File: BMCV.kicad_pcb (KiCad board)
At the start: 4 copper layers, 80 x 108 mm, 349 parts, among them J1 AudioJack2_SwitchT, J10 AudioJack2_SwitchT, J11 AudioJack2_SwitchT, J12 AudioJack2_SwitchT, J13 DebugPins, J14 USB_C_Receptacle_USB2.0_14P, J16 Conn_02x08_Eurorack, J2 AudioJack2_SwitchT, J3 AudioJack2_SwitchT, J4 AudioJack2_SwitchT, J5 AudioJack2_SwitchT, J6 AudioJack2_SwitchT, J7 AudioJack2_SwitchT, J8 AudioJack2_SwitchT, J9 AudioJack2_SwitchT, SW1 TC002-N11AS2XT-RGB, SW10 TC002-N11AS2XT-RGB, SW11 TC002-N11AS2XT-RGB, SW12 TC002-N11AS2XT-RGB, SW13 TC002-N11AS2XT-RGB, SW14 Reset, SW15 Boot, SW2 TC002-N11AS2XT-RGB, SW3 TC002-N11AS2XT-RGB, SW4 TC002-N11AS2XT-RGB, SW5 TC002-N11AS2XT-RGB, SW6 TC002-N11AS2XT-RGB, SW7 TC002-N11AS2XT-RGB, SW8 TC002-N11AS2XT-RGB, SW9 TC002-N11AS2XT-RGB, U1 PEL12T-4225S-S1024, U10 WS2811F, U11 WS2811F, U12 WS2811F, U13 WS2811F, U14 WS2811F, U15 WS2811F, U16 WS2811F, U17 WS2811F, U18 WS2811F, U19 WS2811F, U2 PEL12T-4225S-S1024, U20 WS2811F, U21 WS2811F, U22 WS2811F, U23 WS2811F, U24 WS2811F, U25 WS2811F, U26 WS2811F, U27 WS2811F, U28 WS2811F, U29 WS2811F, U3 PEL12T-4225S-S1024, U30 MCP23S17_SS, U31 MCP23S17_SS, U32 TXS0108EPW, U33 AD7367-5, U34 AD5734R, U35 AD5734R, U36 STM32G474CETx, U38 OPA4171, U39 OPA4171, U4 PEL12T-4225S-S1024, U40 OPA4171, U41 TLV76733, U5 PEL12T-4225S-S1024, U6 PEL12T-4225S-S1024, U7 PEL12T-4225S-S1024, U8 PEL12T-4225S-S1024, U9 WS2811F, Y1 38.4MHz 10pF

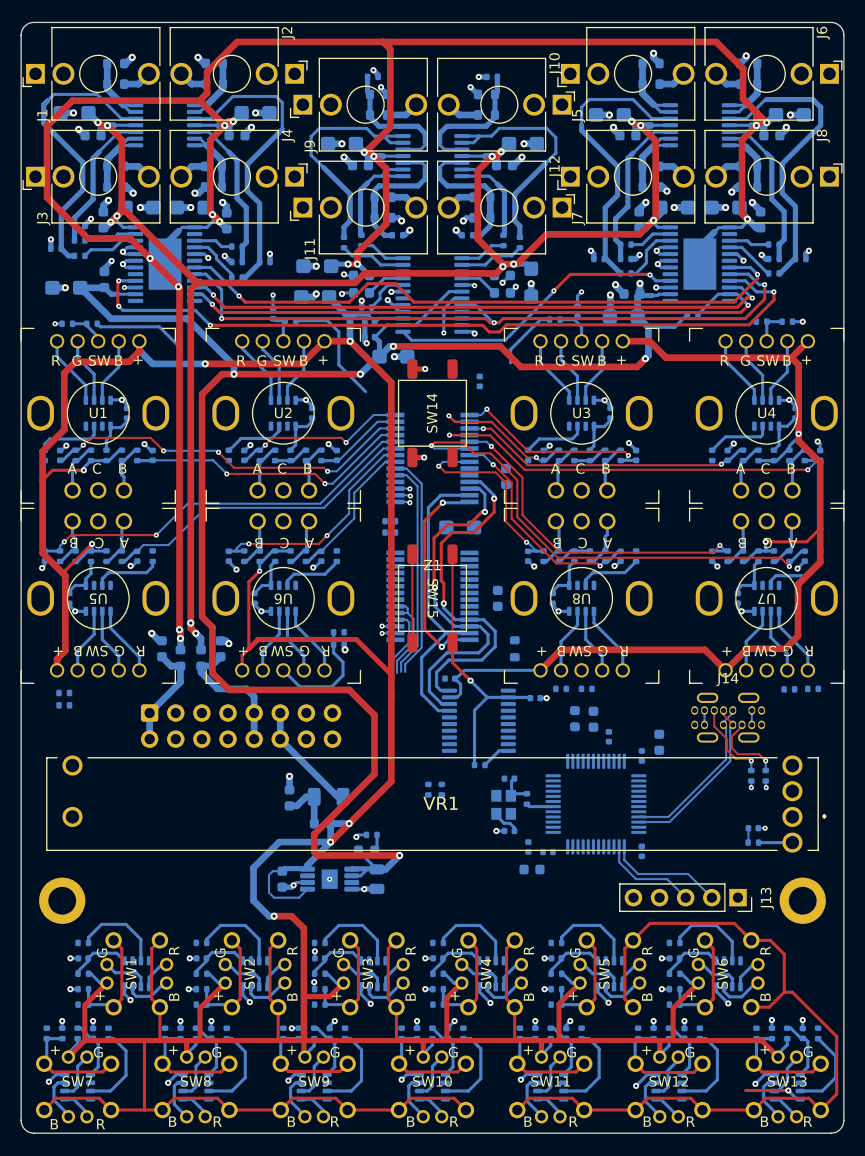
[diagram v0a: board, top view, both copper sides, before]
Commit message: switches & led data routing
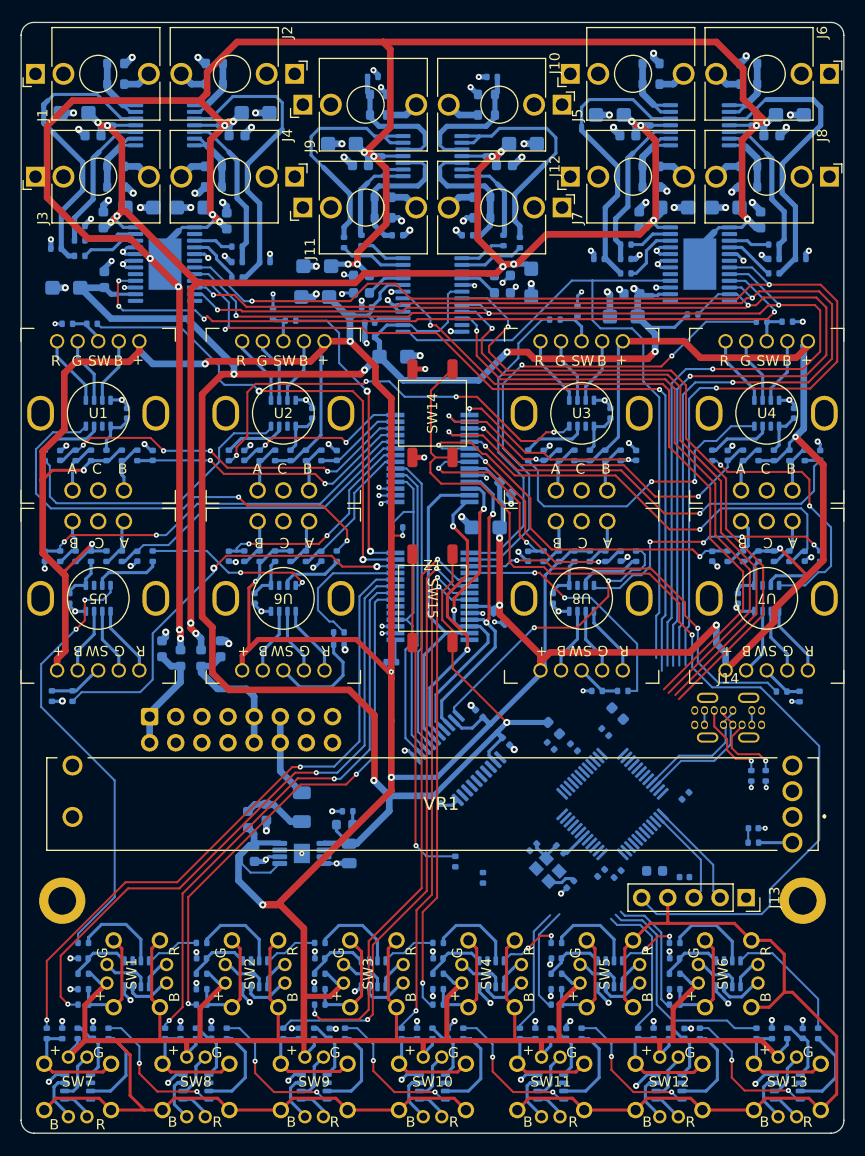
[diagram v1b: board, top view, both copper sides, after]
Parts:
- removed R164: 100, Resistor_SMD:R_0603_1608Metric
- C9: footprint Capacitor_SMD:C_0603_1608Metric -> Capacitor_SMD:C_0402_1005Metric
- moved C11 52.1 mm to (94.5, 113.1), turned to 180 degrees
- moved R160 12.6 mm to (66.0, 92.2), turned to 0 degrees
- moved C7 11.9 mm to (91.6, 112.5), turned to 0 degrees
- moved R163 9.46 mm to (74.9, 113.2)
- moved C1 7.86 mm to (83.4, 113.8), turned to -135 degrees
- moved Y1 7.64 mm to (81.2, 112.4), turned to 135 degrees
- moved C4 7.51 mm to (86.4, 112.7), turned to -135 degrees
- moved R3 7.46 mm to (72.2, 111.6), turned to 90 degrees
- moved FB2 7.26 mm to (52.0, 107.5), turned to 90 degrees
- moved C3 7.10 mm to (88.0, 112.8), turned to -135 degrees
- moved C2 7.06 mm to (79.8, 110.2), turned to -135 degrees
- moved C5 6.87 mm to (94.6, 105.2), turned to 45 degrees
- moved R136 6.00 mm to (88.5, 95.0), turned to 0 degrees
- moved R41 5.86 mm to (82.4, 110.4), turned to -45 degrees
- moved R162 5.38 mm to (70.4, 105.6), turned to 135 degrees
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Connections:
- R140 pad 2: unconnected-(R140-Pad2) -> BTN_MCU_2
- R141 pad 2: unconnected-(R141-Pad2) -> BTN_MCU_5
- R142 pad 2: unconnected-(R142-Pad2) -> BTN_MCU_4
- R143 pad 2: unconnected-(R143-Pad2) -> BTN_MCU_3
- R144 pad 2: unconnected-(R144-Pad2) -> BTN_MCP_8
- R145 pad 2: /Buttons/BUTTON_MCU_5 -> BTN_MCP_7
- R146 pad 2: /Buttons/BUTTON_MCU_4 -> BTN_MCP_6
- R147 pad 2: /Buttons/BUTTON_MCU_3 -> BTN_MCP_5
- R148 pad 2: unconnected-(R148-Pad2) -> BTN_MCU_1
- R150 pad 2: unconnected-(R150-Pad2) -> BTN_MCP_4
- R152 pad 2: unconnected-(R152-Pad2) -> BTN_MCP_3
- R154 pad 2: /Buttons/BUTTON_MCU_2 -> BTN_MCP_2
- R156 pad 2: /Buttons/BUTTON_MCU_1 -> BTN_MCP_1
- R42 pad 2: unconnected-(R42-Pad2) -> Net-(U10-DO)
- R64 pad 2: unconnected-(R64-Pad2) -> Net-(U11-DO)
- R65 pad 2: unconnected-(R65-Pad2) -> Net-(U12-DO)
- R66 pad 2: unconnected-(R66-Pad2) -> Net-(U15-DO)
- R67 pad 2: unconnected-(R67-Pad2) -> WSDATA_5V
- R68 pad 2: unconnected-(R68-Pad2) -> Net-(U16-DO)
- R69 pad 2: unconnected-(R69-Pad2) -> Net-(U9-DO)
- R70 pad 2: unconnected-(R70-Pad2) -> Net-(U14-DO)
- R71 pad 2: unconnected-(R71-Pad2) -> WSDATA_5V_BOTTOM
- R72 pad 2: unconnected-(R72-Pad2) -> Net-(U17-DO)
- R73 pad 2: unconnected-(R73-Pad2) -> Net-(U18-DO)
- R74 pad 2: unconnected-(R74-Pad2) -> Net-(U19-DO)
- R75 pad 2: unconnected-(R75-Pad2) -> Net-(U20-DO)
- R76 pad 2: unconnected-(R76-Pad2) -> Net-(U21-DO)
- R77 pad 2: unconnected-(R77-Pad2) -> Net-(U22-DO)
- R78 pad 2: unconnected-(R78-Pad2) -> Net-(U29-DO)
- R79 pad 2: unconnected-(R79-Pad2) -> Net-(U28-DO)
- R80 pad 2: unconnected-(R80-Pad2) -> Net-(U27-DO)
- R81 pad 2: unconnected-(R81-Pad2) -> Net-(U26-DO)
- R82 pad 2: unconnected-(R82-Pad2) -> Net-(U25-DO)
- R83 pad 2: unconnected-(R83-Pad2) -> Net-(U24-DO)
- U10 pad 5: unconnected-(U10-DO-Pad5) -> Net-(U10-DO)
- U11 pad 5: unconnected-(U11-DO-Pad5) -> Net-(U11-DO)
- U12 pad 5: unconnected-(U12-DO-Pad5) -> Net-(U12-DO)
- U13 pad 5: unconnected-(U13-DO-Pad5) -> WSDATA_5V_BOTTOM
- U14 pad 5: unconnected-(U14-DO-Pad5) -> Net-(U14-DO)
- U15 pad 5: unconnected-(U15-DO-Pad5) -> Net-(U15-DO)
- U16 pad 5: unconnected-(U16-DO-Pad5) -> Net-(U16-DO)
- U17 pad 5: unconnected-(U17-DO-Pad5) -> Net-(U17-DO)
- U18 pad 5: unconnected-(U18-DO-Pad5) -> Net-(U18-DO)
- U19 pad 5: unconnected-(U19-DO-Pad5) -> Net-(U19-DO)
- U20 pad 5: unconnected-(U20-DO-Pad5) -> Net-(U20-DO)
- U21 pad 5: unconnected-(U21-DO-Pad5) -> Net-(U21-DO)
- U22 pad 5: unconnected-(U22-DO-Pad5) -> Net-(U22-DO)
- U24 pad 5: unconnected-(U24-DO-Pad5) -> Net-(U24-DO)
- U25 pad 5: unconnected-(U25-DO-Pad5) -> Net-(U25-DO)
- U26 pad 5: unconnected-(U26-DO-Pad5) -> Net-(U26-DO)
- U27 pad 5: unconnected-(U27-DO-Pad5) -> Net-(U27-DO)
- U28 pad 5: unconnected-(U28-DO-Pad5) -> Net-(U28-DO)
- U29 pad 5: unconnected-(U29-DO-Pad5) -> Net-(U29-DO)
- U30 pad 1: ENC_1_SW -> ENC_2_SW
- U30 pad 19: MCP_5V_BTNINT -> unconnected-(U30-INTB-Pad19)
- U30 pad 2: ENC_2_SW -> ENC_1_SW
- U30 pad 20: MCP_5V_BTNINT -> unconnected-(U30-INTA-Pad20)
- U30 pad 21: unconnected-(U30-GPA0-Pad21) -> BTN_MCP_2
- U30 pad 22: unconnected-(U30-GPA1-Pad22) -> BTN_MCP_6
- U30 pad 23: unconnected-(U30-GPA2-Pad23) -> BTN_MCP_1
- U30 pad 24: unconnected-(U30-GPA3-Pad24) -> BTN_MCP_5
- U30 pad 25: unconnected-(U30-GPA4-Pad25) -> ENC_6_SW
- U30 pad 26: unconnected-(U30-GPA5-Pad26) -> ENC_5_SW
- U30 pad 27: unconnected-(U30-GPA6-Pad27) -> ENC_4_SW
- U30 pad 28: unconnected-(U30-GPA7-Pad28) -> ENC_3_SW
- U30 pad 3: ENC_3_SW -> ENC_7_SW
- U30 pad 4: ENC_4_SW -> ENC_8_SW
- U30 pad 5: ENC_5_SW -> BTN_MCP_3
- U30 pad 6: ENC_6_SW -> BTN_MCP_7
- U30 pad 7: ENC_7_SW -> BTN_MCP_8
- U30 pad 8: ENC_8_SW -> BTN_MCP_4
- U31 pad 5: ENC_7_B -> ENC_7_A
- U31 pad 6: ENC_7_A -> ENC_7_B
- U32 pad 1: MCP_CS -> WSDATA
- U32 pad 12: WSDATA_5V -> MCP_5V_RESET
- U32 pad 13: unconnected-(U32-B7-Pad13) -> MCP_5V_ENCINT_A
- U32 pad 14: unconnected-(U32-B6-Pad14) -> MCP_5V_ENCINT_B
- U32 pad 15: MCP_5V_RESET -> MCP_5V_SI
- U32 pad 16: unconnected-(U32-B4-Pad16) -> MCP_5V_SO
- U32 pad 17: MCP_5V_SI -> MCP_5V_SCK
- U32 pad 18: MCP_5V_SCK -> MCP_5V_CS
- U32 pad 20: MCP_5V_CS -> WSDATA_5V
- U32 pad 3: MCP_SCK -> MCP_CS
- U32 pad 4: MCP_SI -> MCP_SCK
- U32 pad 5: unconnected-(U32-A4-Pad5) -> MCP_SO
- U32 pad 6: MCP_RESET -> MCP_SI
- U32 pad 7: unconnected-(U32-A6-Pad7) -> MCP_ENCINT_B
- U32 pad 8: unconnected-(U32-A7-Pad8) -> MCP_ENCINT_A
- U32 pad 9: WSDATA -> MCP_RESET
- U36 pad 10: unconnected-(U36-PA2-Pad10) -> ADC_DAC_SDO
- U36 pad 11: unconnected-(U36-PA3-Pad11) -> ADC_DAC_SDIN
- U36 pad 12: unconnected-(U36-PA4-Pad12) -> ADC_DAC_SCLK
- U36 pad 13: unconnected-(U36-PA5-Pad13) -> ADC_CS
- U36 pad 14: unconnected-(U36-PA6-Pad14) -> ADC_ADDR
- U36 pad 15: unconnected-(U36-PA7-Pad15) -> ADC_CNVST
- U36 pad 25: unconnected-(U36-PB11-Pad25) -> BTN_MCU_1
- U36 pad 26: unconnected-(U36-PB12-Pad26) -> BTN_MCU_2
- U36 pad 27: unconnected-(U36-PB13-Pad27) -> BTN_MCU_3
- U36 pad 28: unconnected-(U36-PB14-Pad28) -> BTN_MCU_4
- U36 pad 29: unconnected-(U36-PB15-Pad29) -> BTN_MCU_5
- U36 pad 30: unconnected-(U36-PA8-Pad30) -> ADC_BUSY
- U36 pad 31: unconnected-(U36-PA9-Pad31) -> DAC_1_SYNC
- U36 pad 32: unconnected-(U36-PA10-Pad32) -> DAC_1_LDAC
- U36 pad 39: unconnected-(U36-PA15-Pad39) -> DAC_1_CLR
- U9 pad 5: unconnected-(U9-DO-Pad5) -> Net-(U9-DO)
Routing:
- net NRST: track 0.00 -> 98.6 mm, vias 0 -> 1
- net ADC_DAC_SDIN: track 0.00 -> 79.5 mm, vias 0 -> 2
- net +5V: track 576.9 -> 656.0 mm, vias 10 -> 14
- net ADC_ADDR: track 0.00 -> 65.2 mm, vias 0 -> 1
- net BTN_MCP_5: track 0.00 -> 64.1 mm, vias 0 -> 2
- net ADC_CNVST: track 0.00 -> 63.4 mm, vias 0 -> 1
- net ADC_CS: track 4.54 -> 66.8 mm
- net BTN_MCP_1: track 0.00 -> 61.8 mm, vias 0 -> 2
- net ADC_BUSY: track 0.00 -> 61.1 mm, vias 0 -> 1
- net BTN_MCP_7: track 0.00 -> 59.1 mm, vias 0 -> 2
- net BTN_MCP_3: track 0.00 -> 57.3 mm, vias 0 -> 2
- net DAC_1_SYNC: track 62.0 -> 118.8 mm, vias 2 -> 3
- net DAC_1_LDAC: track 58.1 -> 114.3 mm, vias 2 -> 3
- net DAC_1_CLR: track 61.1 -> 116.8 mm, vias 2 -> 3
- net BTN_MCP_6: track 0.00 -> 55.1 mm, vias 0 -> 2
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
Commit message: completed routing and mcu pins
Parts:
- removed R41: 33, Resistor_SMD:R_0402_1005Metric
- added C95: 100n, Capacitor_SMD:C_0402_1005Metric, B.Cu at (95.0, 107.0)
- added J15: Conn_01x02, TestPoint:TestPoint_2Pads_Pitch2.54mm_Drill0.8mm, B.Cu at (73.6, 114.2)
- added U37: MB85RS64PNF-G-JNERE1, Package_SO:SSOP-8_3.9x5.05mm_P1.27mm, B.Cu at (98.5, 108.8)
- moved C11 20.8 mm to (107.0, 96.5), turned to -90 degrees
- moved R158 7.98 mm to (96.7, 103.2), turned to -90 degrees
- moved C46 6.05 mm to (99.0, 102.7)
- moved R163 3.88 mm to (75.6, 109.3)
- moved R3 2.92 mm to (74.1, 109.3)
- moved C1 1.62 mm to (84.0, 112.3), turned to -90 degrees
- moved C2 1.57 mm to (81.2, 109.6), turned to 180 degrees
- moved C10 0.99 mm to (87.2, 97.7)
- moved Y1 0.83 mm to (81.7, 111.7), turned to 180 degrees
- moved C5 0.54 mm to (94.3, 104.8)
- moved C4 0.54 mm to (86.9, 112.5)
- moved C7 0.52 mm to (91.1, 112.3)
- moved C6 0.34 mm to (86.5, 99.2)
- moved C3 0.32 mm to (88.1, 113.1)
- moved C8 0.24 mm to (84.0, 100.3), turned to 45 degrees
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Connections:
- C2 pad 1: Net-(C2-Pad1) -> HSE_OUT
- R163 pad 1: BOOT -> Net-(R163-Pad1)
- R163 pad 2: Net-(U36-PB8) -> BOOT
- R3 pad 2: BOOT -> Net-(R163-Pad1)
- SW15 pad 2: BOOT -> Net-(R163-Pad1)
- U36 pad 10: ADC_DAC_SDO -> MCP_ENCINT_A
- U36 pad 11: ADC_DAC_SDIN -> MCP_ENCINT_B
- U36 pad 12: ADC_DAC_SCLK -> MCP_CS
- U36 pad 13: ADC_CS -> MCP_SCK
- U36 pad 14: ADC_ADDR -> MCP_SO
- U36 pad 15: ADC_CNVST -> MCP_SI
- U36 pad 16: unconnected-(U36-PB0-Pad16) -> MCP_RESET
- U36 pad 17: unconnected-(U36-PB1-Pad17) -> WSDATA
- U36 pad 18: unconnected-(U36-PB2-Pad18) -> ADC_CS
- U36 pad 2: unconnected-(U36-PC13-Pad2) -> BTN_MCU_2
- U36 pad 22: unconnected-(U36-PB10-Pad22) -> ADC_CNVST
- U36 pad 25: BTN_MCU_1 -> ADC_ADDR
- U36 pad 26: BTN_MCU_2 -> ADC_BUSY
- U36 pad 27: BTN_MCU_3 -> ADC_DAC_SCLK
- U36 pad 28: BTN_MCU_4 -> ADC_DAC_SDO
- U36 pad 29: BTN_MCU_5 -> ADC_DAC_SDIN
- U36 pad 3: unconnected-(U36-PC14-Pad3) -> BTN_MCU_5
- U36 pad 30: ADC_BUSY -> DAC_1_CLR
- U36 pad 31: DAC_1_SYNC -> DAC_1_LDAC
- U36 pad 32: DAC_1_LDAC -> DAC_1_SYNC
- U36 pad 39: DAC_1_CLR -> EXP_CS
- U36 pad 4: unconnected-(U36-PC15-Pad4) -> BTN_MCU_4
- U36 pad 43: unconnected-(U36-PB6-Pad43) -> PB6
- U36 pad 44: unconnected-(U36-PB7-Pad44) -> PB7
- U36 pad 45: Net-(U36-PB8) -> BOOT
- U36 pad 46: unconnected-(U36-PB9-Pad46) -> BTN_MCU_1
- U36 pad 8: unconnected-(U36-PA0-Pad8) -> BTN_MCU_3
- VR1 pad 1: +3.3VA -> +3.3V
- Y1 pad 3: Net-(C2-Pad1) -> HSE_OUT
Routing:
- net +3.3V: track 292.2 -> 369.6 mm, vias 7 -> 10
- net Net-(R163-Pad1): track 0.00 -> 42.4 mm, vias 0 -> 1
- net GND: track 201.5 -> 230.0 mm, vias 167 -> 193
- net PB6: track 0.00 -> 25.1 mm, vias 0 -> 1
- net PB7: track 0.00 -> 20.4 mm, vias 0 -> 1
- net NRST: track 98.6 -> 117.6 mm, vias 1 -> 2
- net BOOT: track 32.7 -> 16.6 mm, vias 1 -> 2
- net ADC1_IN2_SLIDER: track 1.41 -> 17.1 mm, vias 0 -> 2
- net ADC_CS: track 66.8 -> 82.0 mm, vias 1 -> 2
- net EXP_MISO: track 0.00 -> 14.4 mm
- net MCP_RESET: track 0.00 -> 14.0 mm, vias 0 -> 2
- net BTN_MCU_3: track 12.2 -> 25.5 mm, vias 0 -> 2
- net ADC_CNVST: track 63.4 -> 76.2 mm, vias 1 -> 2
- net DAC_1_LDAC: track 114.3 -> 126.5 mm
- net ADC_DAC_SCLK: track 120.5 -> 132.6 mm, vias 4 -> 6
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
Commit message: cleanup
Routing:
- net Net-(VR1-WIPER): track 12.2 -> 10.8 mm
- net EXP_SCLK: track 7.25 -> 6.75 mm
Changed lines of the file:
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@@
 	)
 	(segment
-		(start 90.175 112.2)
-		(end 90.325 112.35)
-		(width 0.5)
-		(layer "B.Cu")
-		(net 39)
-	)
-	(segment
 		(start 92.125 56.425)
 		(end 93.125 56.425)
@@
 	)
 	(segment
-		(start 100.790523 107.357502)
-		(end 100.790523 107.359477)
-		(width 0.2)
-		(layer "B.Cu")
-		(net 39)
-	)
-	(segment
 		(start 91.4 56.55)
 		(end 92 56.55)
@@
 	)
 	(segment
-		(start 96.109477 110.242498)
-		(end 96.157502 110.242498)
-		(width 0.2)
-		(layer "B.Cu")
-		(net 39)
-	)
-	(segment
 		(start 83.943153 97.943153)
 		(end 85.75 99.75)
@@
 	)
 	(segment
-		(start 94.660589 107.289411)
-		(end 94.55 107.178822)
-		(width 0.3)
-		(layer "B.Cu")
-		(net 39)
-	)
-	(segment
 		(start 50.7 63.35)
 		(end 46.15 58.8)
@@
 	)
 	(segment
-		(start 80.67 109.6)
-		(end 80.72 109.55)
-		(width 0.3)
-		(layer "B.Cu")
-		(net 65)
-	)
-	(segment
 		(start 40.9 46.6)
 		(end 40.3 46)
@@
 	)
 	(segment
-		(start 102.41 103.75)
-		(end 102.4 103.76)
-		(width 0.2)
-		(layer "B.Cu")
-		(net 65)
-	)
-	(segment
 		(start 86.425 113.675)
 		(end 86.560589 113.539411)
@@
 	)
 	(segment
-		(start 101.688549 108.255528)
-		(end 101.688549 108.261451)
-		(width 0.3)
-		(layer "B.Cu")
-		(net 65)
-	)
-	(segment
 		(start 74.4 37)
 		(end 73.7 36.3)
@@
 	)
 	(segment
-		(start 96.65 102.69)
-		(end 96.64 102.7)
-		(width 0.2)
-		(layer "B.Cu")
-		(net 110)
-	)
-	(segment
-		(start 98.57 102.7)
-		(end 98.56 102.69)
-		(width 0.2)
-		(layer "B.Cu")
-		(net 110)
-	)
-	(segment
 		(start 40.3 68.8)
 		(end 39.7 69.4)
@@
 	)
 	(segment
-		(start 104.15 109.75)
-		(end 105 109.75)
-		(width 0.2)
-		(layer "B.Cu")
-		(net 255)
-	)
-	(segment
-		(start 104.42 109.75)
-		(end 105 109.75)
-		(width 0.3)
-		(layer "B.Cu")
-		(net 255)
-	)
-	(segment
 		(start 39.412501 57.512501)
 		(end 39.5 57.6)
@@
 	)
 	(segment
-		(start 97.007502 111.140523)
-		(end 96.648025 111.5)
-		(width 0.2)
-		(layer "B.Cu")
-		(net 369)
-	)
-	(segment
